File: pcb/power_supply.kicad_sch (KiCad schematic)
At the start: 0 parts

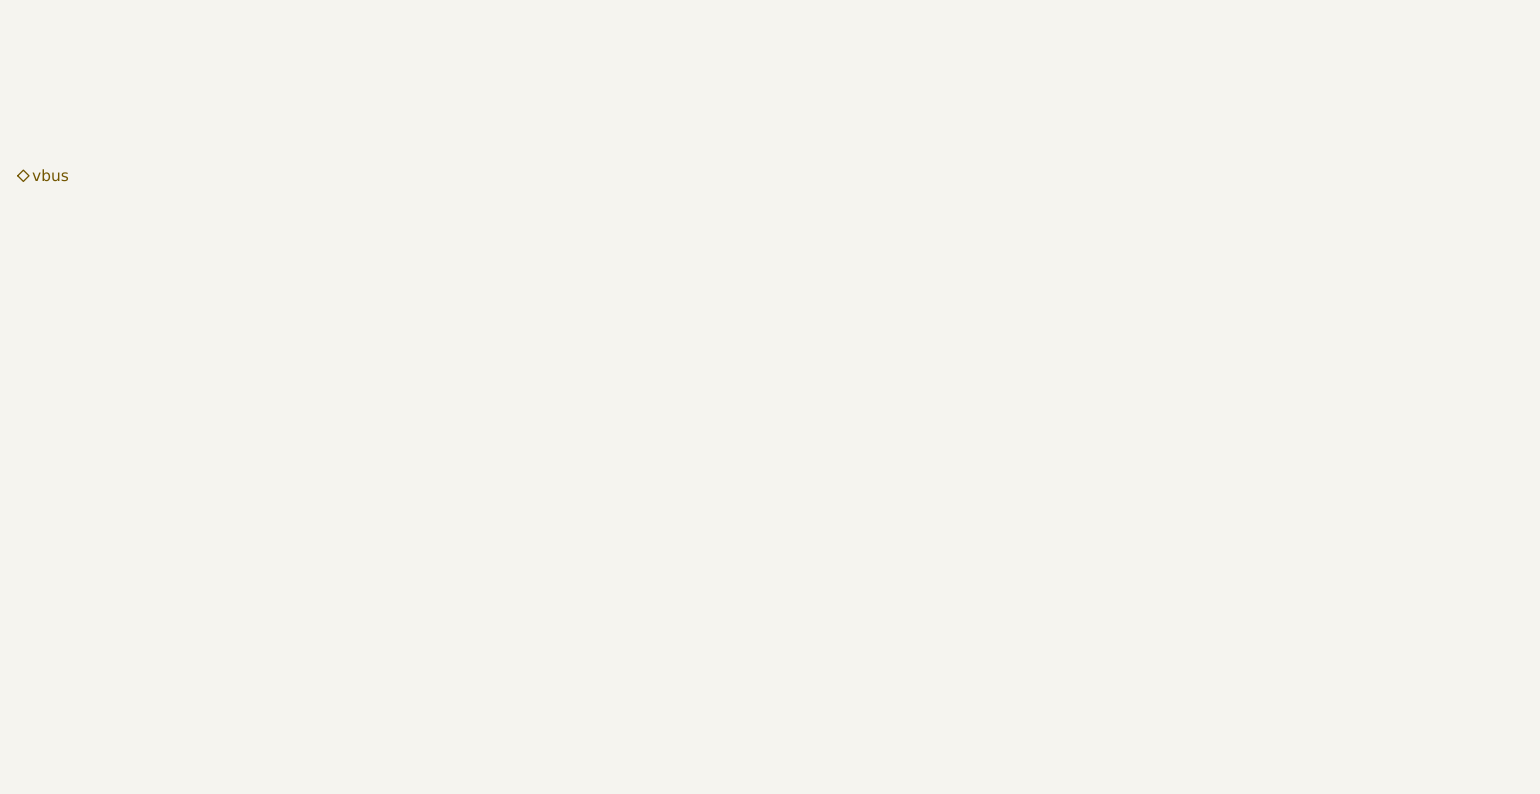
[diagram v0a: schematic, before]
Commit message: Add power supply circuit and MCU symbol.
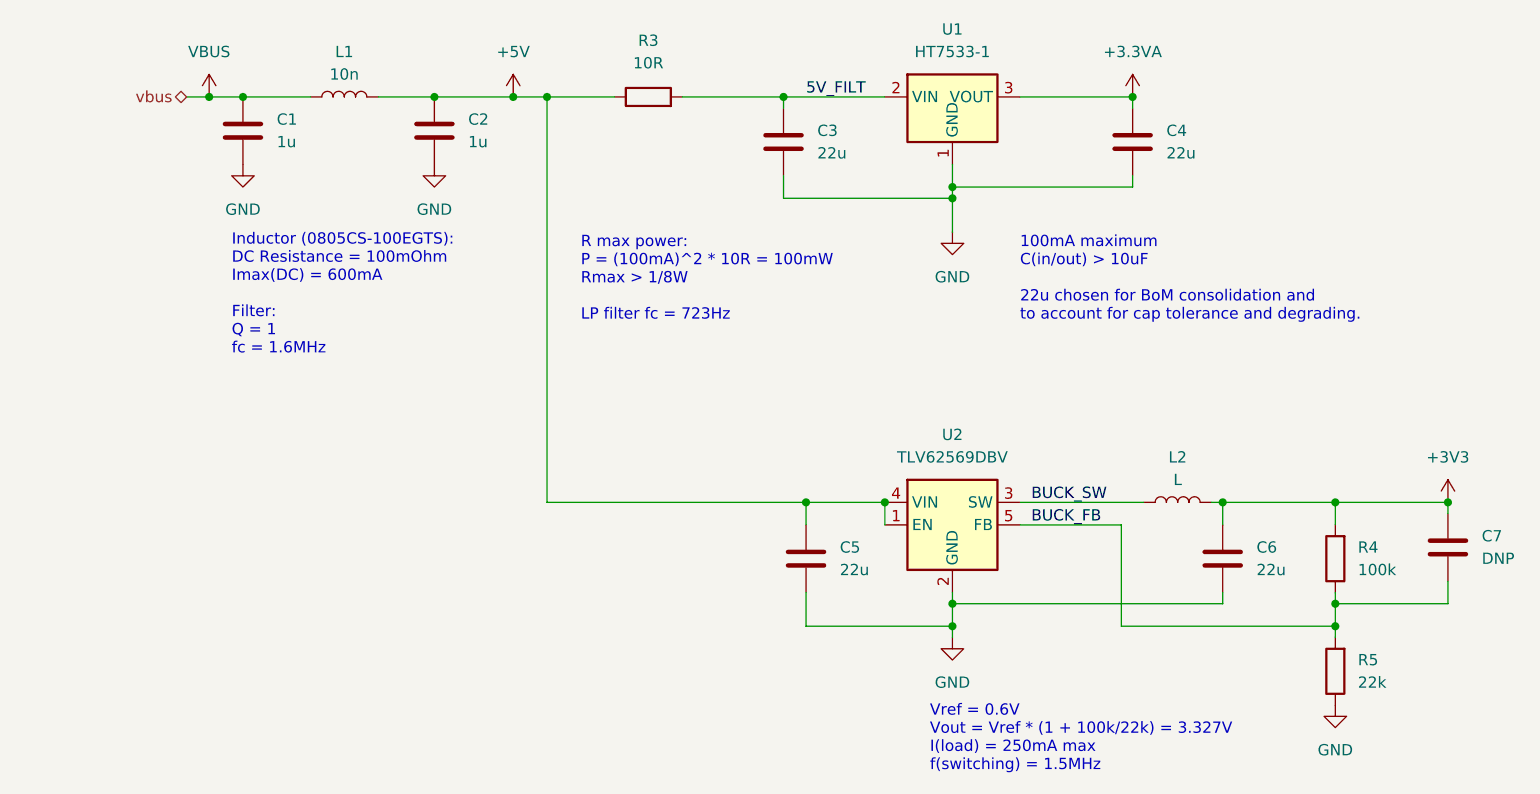
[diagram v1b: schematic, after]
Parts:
- added C1, C2: 1u, Capacitor_SMD:C_0805_2012Metric, symbol Device:C
- added C3, C4, C5, C6: 22u, Capacitor_SMD:C_0805_2012Metric, symbol Device:C
- added C7: DNP, Capacitor_SMD:C_0805_2012Metric, symbol Device:C
- added L1: 10n, Inductor_SMD:L_0805_2012Metric, symbol Device:L
- added L2: L, symbol Device:L
- added R3: 10R, Resistor_SMD:R_0805_2012Metric, symbol Device:R
- added R4: 100k, Resistor_SMD:R_0805_2012Metric, symbol Device:R
- added R5: 22k, Resistor_SMD:R_0805_2012Metric, symbol Device:R
- added U1: HT7533-1, Package_TO_SOT_SMD:SOT-89-3, symbol Regulator_Linear:HT75xx-1-SOT89_1
- added U2: TLV62569DBV, Package_TO_SOT_SMD:SOT-23-5, symbol Regulator_Switching:TLV62569DBV
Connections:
- new net +3.3VA: C4.1, U1.3 (VOUT)
- new net +3V3: C6.1, C7.1, L2.2, R4.2
- new net +5V: C2.1, C5.1, L1.2, R3.1, U2.1 (EN), U2.4 (VIN)
- new net 5V_FILT: C3.1, R3.2, U1.2 (VIN)
- new net BUCK_FB: C7.2, R4.1, R5.2, U2.5 (FB)
- new net BUCK_SW: L2.1, U2.3 (SW)
- new net GND: C1.2, C2.2, C3.2, C4.2, C5.2, C6.2, R5.1, U1.1 (GND), U2.2 (GND)
- new net VBUS: C1.1, L1.1
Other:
- note added: "100mA maximum C(in/out) > 10uF 22u chosen for BoM consolidation and to account for cap tolerance and degrading."
- note added: "Inductor (0805CS-100EGTS): DC Resistance = 100mOhm Imax(DC) = 600mA Filter: Q = 1 fc = 1.6MHz"
- note added: "R max power: P = (100mA)^2 * 10R = 100mW Rmax > 1/8W LP filter fc = 723Hz"
- note added: "Vref = 0.6V Vout = Vref * (1 + 100k/22k) = 3.327V I(load) = 250mA max f(switching) = 1.5MHz"
